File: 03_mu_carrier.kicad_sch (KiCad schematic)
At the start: 155 parts, among them J10 Amphenol MDT420M01001 M-key N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, J8 DNP Mu SIO UART debug header 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, Q750 BSS138 fail-off EN/UVLO clamp, Q751 BSS138 active-high enable rel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, SW2 Mu Power, SW3 Mu Reset, U6 TPS56637RPAR VSYS -> SYS_5V (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, U7 TPS56637RPAR VSYS -> SYS_3V3 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, U750 TPS552892RYQR 12V buck-boost, U769 SN74LVC1G08DBVR qualified hos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, U770 TPS2553DDBVR internal host VB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, U771 TPS3897ADRYR internal VBUS su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, U772 TPS22975NDSGR switched PCIe e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, U773 TPS56637RPAR VSYS -> PCIE_3V3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

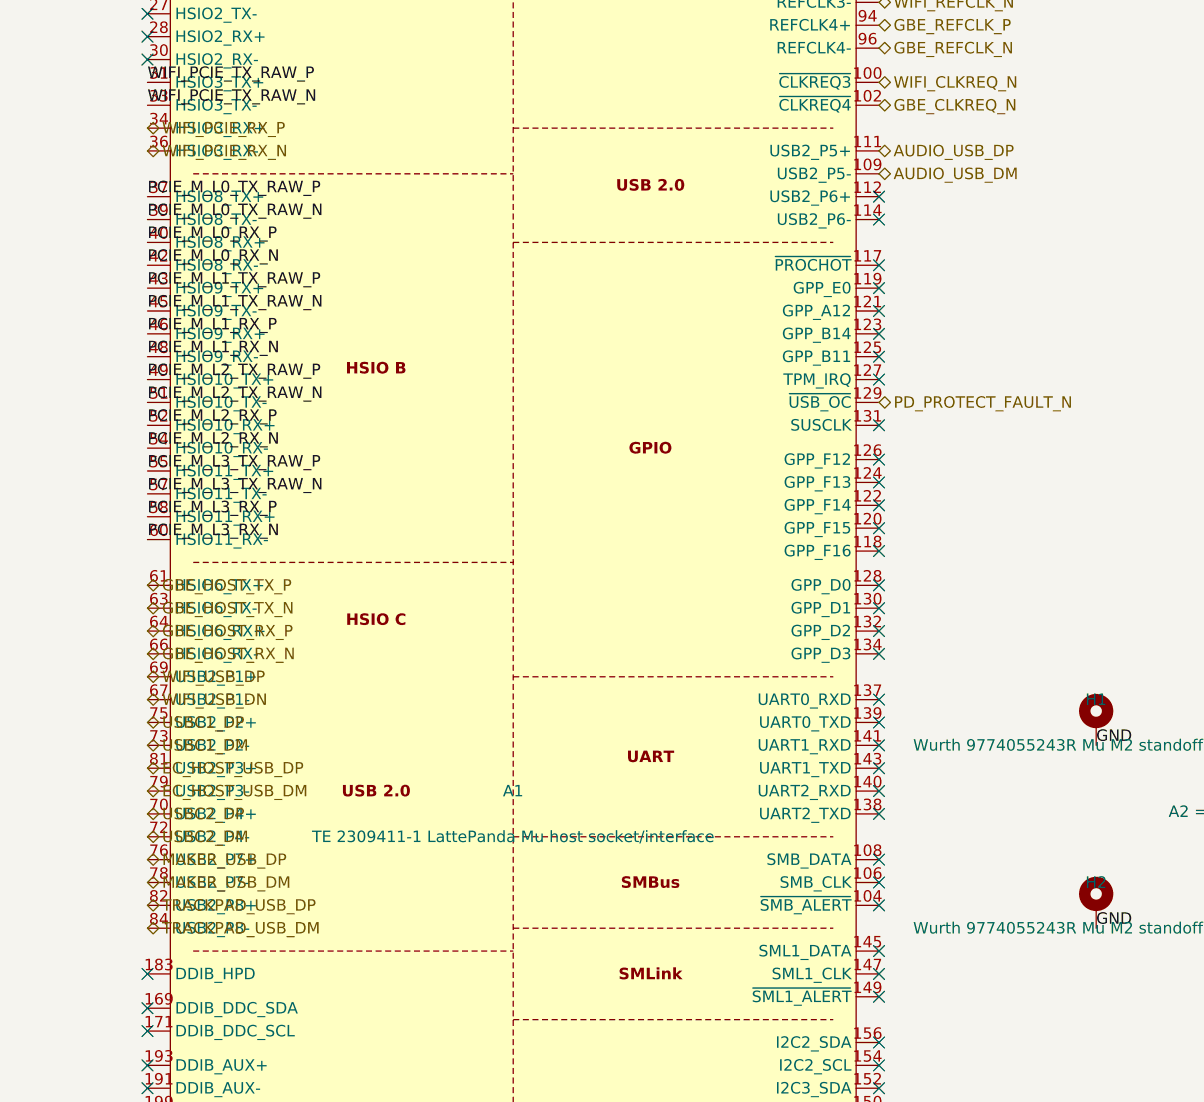
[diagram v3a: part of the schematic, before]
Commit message: get the main boards ready for routing
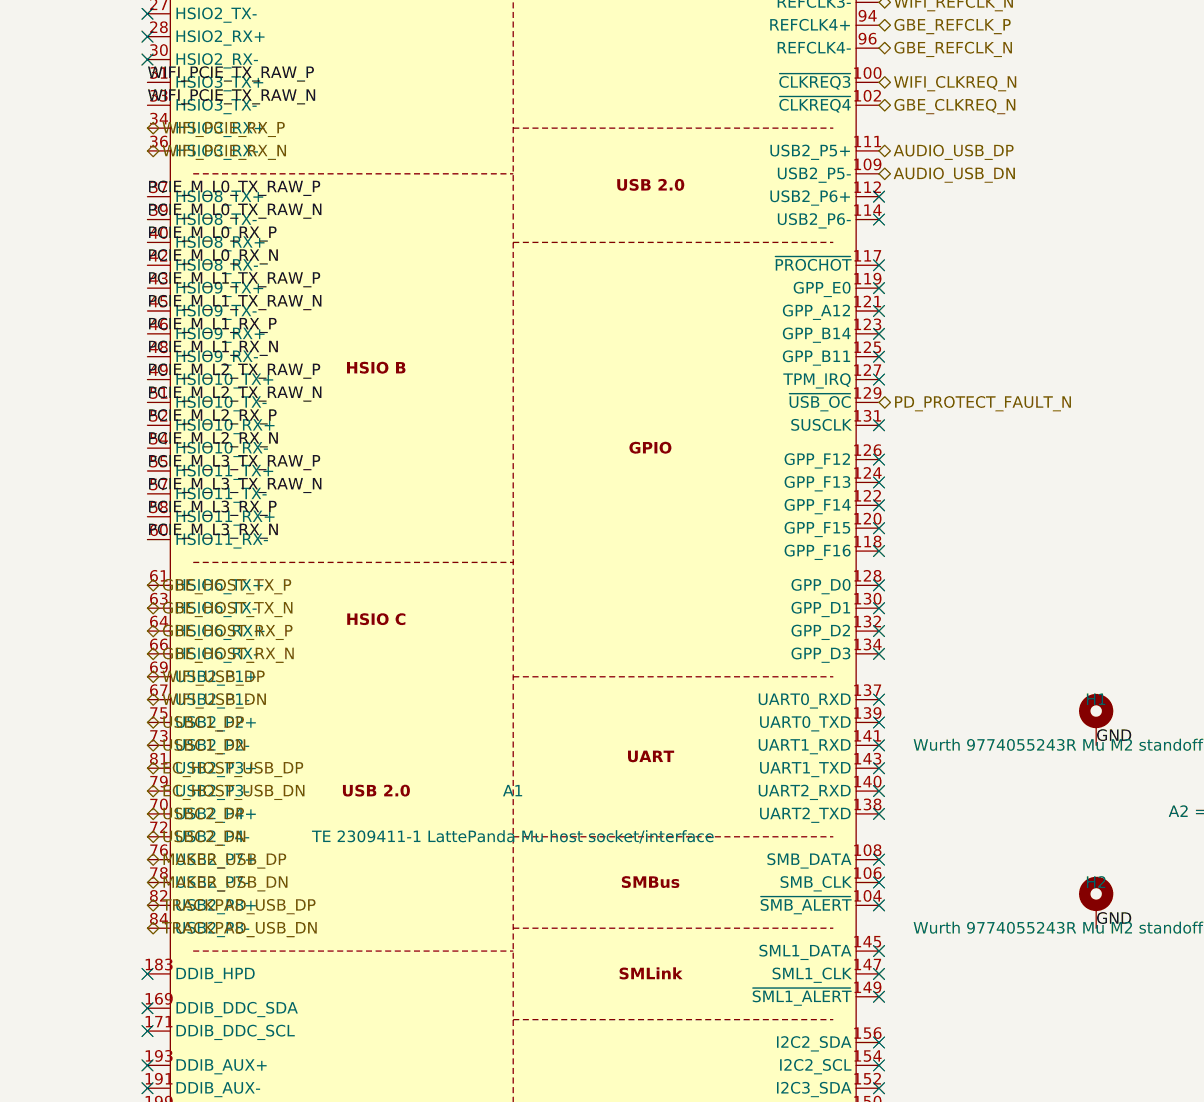
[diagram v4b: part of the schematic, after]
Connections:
- net AUDIO_USB_DM renamed AUDIO_USB_DN
- net EC_HOST_USB_DM renamed EC_HOST_USB_DN
- net MAKER_USB_DM renamed MAKER_USB_DN
- net TRACKPAD_USB_DM renamed TRACKPAD_USB_DN
- net USBC1_DM renamed USBC1_DN
- net USBC2_DM renamed USBC2_DN
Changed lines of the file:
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@@
 (no_connect (at 200.66 187.96))
 (no_connect (at 200.66 185.42))
-(hierarchical_label "AUDIO_USB_DM"
+(hierarchical_label "AUDIO_USB_DN"
   (shape bidirectional)
   (at 200.66 109.22 0)
@@
   (effects (font (size 1.27 1.27)) (justify left bottom))
 )
-(hierarchical_label "USBC2_DM"
+(hierarchical_label "USBC2_DN"
   (shape bidirectional)
   (at 119.38 182.88 0)
   (effects (font (size 1.27 1.27)) (justify left bottom))
 )
-(hierarchical_label "USBC1_DM"
+(hierarchical_label "USBC1_DN"
   (shape bidirectional)
   (at 119.38 172.72 0)
@@
   (effects (font (size 1.27 1.27)) (justify left bottom))
 )
-(hierarchical_label "MAKER_USB_DM"
+(hierarchical_label "MAKER_USB_DN"
   (shape bidirectional)
   (at 119.38 187.96 0)
   (effects (font (size 1.27 1.27)) (justify left bottom))
 )
-(hierarchical_label "EC_HOST_USB_DM"
+(hierarchical_label "EC_HOST_USB_DN"
   (shape bidirectional)
   (at 119.38 177.8 0)
@@
   (effects (font (size 1.27 1.27)) (justify left bottom))
 )
-(hierarchical_label "TRACKPAD_USB_DM"
+(hierarchical_label "TRACKPAD_USB_DN"
   (shape bidirectional)
   (at 119.38 193.04 0)

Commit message: fix audit issues and move some connectors
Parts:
- C762: footprint Capacitor_SMD:CP_Elec_6.3x5.8 -> Capacitor_SMD:CP_Elec_6.3x7.7
- C771: value 4.7n COMP -> 220n 50V X7R COMP; MPN GRM188R71H472KA01 -> C0603C224K5RACTU; Manufacturer Murata -> KEMET
- C772: value 100p C0G COMP HF -> 1n 50V C0G COMP HF; MPN GRM1885C1H101JA01 -> GRM1885C1H102JA01D
- C782, C834: footprint Capacitor_SMD:C_1206_3216Metric -> Capacitor_SMD:C_1210_3225Metric
- C783, C794, C832: footprint Capacitor_SMD:C_0805_2012Metric -> Capacitor_SMD:C_0603_1608Metric
- C830, C836: footprint Capacitor_SMD:C_1206_3216Metric -> Capacitor_SMD:C_0805_2012Metric
- D1824: value 1N5819HW RTC_BAT diode-OR from MCU_3V3 -> 1N5819HW RTC supply from MCU_3V3; footprint Diode_SMD:Nexperia_CFP3_SOD-123W -> Diode_SMD:D_SOD-123; MPN 1N5819HW -> 1N5819HW-7-F; Manufacturer STMicroelectronics -> Diodes Incorporated
- L750: value 4.7uH 10.1A Isat / 6.9A Irms -> 6.8uH 12.8A Isat30 / 6.8A Irms20; 7mm class; footprint Inductor_SMD:L_Coilcraft_XAL7030-472 -> Inductor_SMD:L_Coilcraft_XAL7070-XXX; MPN XAL7030-472MEC -> XAL7070-682MEC
- R40: MPN RT0603BRD075KL -> RT0603BRD0775KL
- R42, R770: MPN RC0603FR-07169KL -> RC0603FR-07100KL
- R45, R771: MPN RC0603FR-0736K1L -> RC0603FR-07100KL
- R755: value 15k COMP series -> 5.1k 1% COMP series; MPN RC0603FR-0715KL -> RC0603FR-075K1L
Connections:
- net MCU_3V3: now also D1824.2 (A); no longer D1824.1 (K)
- net RTC_BAT: now also D1824.1 (K); no longer D1824.2 (A)

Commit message: fix the center layout and more board issues
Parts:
- removed C40, C41: 10u 50V X7R TPS56637 VIN, Capacitor_SMD:C_1206_3216Metric, symbol Device:C
- removed C42: 100n 50V X7R TPS56637 VIN HF, Capacitor_SMD:C_0603_1608Metric, symbol Device:C
- removed C43: 100n 16V X7R TPS56637 BOOT, Capacitor_SMD:C_0603_1608Metric, symbol Device:C
- removed C44, C45: 22u 16V X7R TPS56637 OUT, Capacitor_SMD:C_1206_3216Metric, symbol Device:C
- removed C768: DNP 2.2n 250V X7R switch-node snubber, Capacitor_SMD:C_0805_2012Metric, symbol Device:C
- removed C794: 1u internal host VBUS switch input, Capacitor_SMD:C_0603_1608Metric, symbol Device:C
- removed C830: 10u internal host VBUS output, Capacitor_SMD:C_0805_2012Metric, symbol Device:C
- removed C834: 47u 6.3V PCIe endpoint rail bulk, Capacitor_SMD:C_1210_3225Metric, symbol Device:C
- removed C835: 100n PCIe endpoint rail HF, Capacitor_SMD:C_0603_1608Metric, symbol Device:C
- removed R761: 100k fail-off gate divider low, Resistor_SMD:R_0603_1608Metric, symbol Device:R
- removed R766: 100k fail-off gate divider high, Resistor_SMD:R_0603_1608Metric, symbol Device:R
- removed R787: 100k 1% TPS56637 EN high (host-active gate), Resistor_SMD:R_0603_1608Metric, symbol Device:R
- removed R788: 100k 1% TPS56637 EN low, Resistor_SMD:R_0603_1608Metric, symbol Device:R
- removed R789: 100k PCIE_3V3_PG pull-up, Resistor_SMD:R_0603_1608Metric, symbol Device:R
- removed U6: TPS56637RPAR VSYS -> SYS_5V (5.10V, 6A class), ducktop2:Texas_RPA0010A_VQFN-HR-10_3x3mm, symbol TPS56637:TPS56637
- removed U771: TPS3897ADRYR internal VBUS supervisor (always-pow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, Package_SON:Texas_USON-6_1x1.45mm_P0.5mm_SMD, symbol TPS3897ADRYR:TPS3897ADRYR
- removed U772: TPS22975NDSGR switched PCIe endpoint 3V3, Package_SON:Texas_DSG0008A_WSON-8-1EP_2x2mm_P0.5mm_EP0.9x1.6mm, symbol TPS22975N:TPS22975N
- removed U773: TPS56637RPAR VSYS -> PCIE_3V3_IN (3.32V, 6A class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, ducktop2:Texas_RPA0010A_VQFN-HR-10_3x3mm, symbol TPS56637:TPS56637
- added C2280: 22u 25V endpoint VCC; effective minimum 4.7u, Capacitor_SMD:C_1210_3225Metric, symbol Device:C
- added C2281: 100n 50V endpoint VDDA, Capacitor_SMD:C_0603_1608Metric, symbol Device:C
- added C2282: 220n 50V X7R endpoint COMP, Capacitor_SMD:C_0603_1608Metric, symbol Device:C
- added C2283: 2.2n 50V C0G endpoint COMP HF, Capacitor_SMD:C_0603_1608Metric, symbol Device:C
- added C2284, C2285: 330u 10V endpoint local reservoir, Capacitor_Tantalum_SMD:CP_EIA-7343-43_Kemet-X, symbol Device:C_Polarized
- added C2286, C778: 100n 50V endpoint input HF, Capacitor_SMD:C_0603_1608Metric, symbol Device:C
- added C2287: 22u 25V endpoint output; TI characterized part, Capacitor_SMD:C_1210_3225Metric, symbol Device:C
- added C2288: 100n 50V endpoint enable gate supply, Capacitor_SMD:C_0603_1608Metric, symbol Device:C
- added C2289: 22n 50V C0G 5% endpoint slew; parallel pair, Capacitor_SMD:C_0805_2012Metric, symbol Device:C
- added C2412: 100n, Capacitor_SMD:C_0603_1608Metric, symbol Device:C
- added C46, C790: 10u 50V X7R TPS56637 VIN, Capacitor_SMD:C_1206_3216Metric, symbol Device:C
- added C47: 100n 16V X7R TPS56637 BOOT, Capacitor_SMD:C_0603_1608Metric, symbol Device:C
- added C48, C792: 22u 25V X7R TPS56637 OUT; TI example part, Capacitor_SMD:C_1210_3225Metric, symbol Device:C
- added C586, C587, C66, C67: 100n 10V X7R Mu USB3 TX AC, Capacitor_SMD:C_0402_1005Metric, symbol Device:C
- added C776, C777: 10u 50V endpoint input, Capacitor_SMD:C_1206_3216Metric, symbol Device:C
- added C791: 100n 50V X7R TPS56637 VIN HF, Capacitor_SMD:C_0603_1608Metric, symbol Device:C
- added H25: M2.5 isolated mainboard mounting hole, MountingHole:MountingHole_2.7mm_M2.5, symbol Mechanical:MountingHole
- added J10: Amphenol MDT420M01001 M-key NVMe socket (PCIe x4), ducktop2:Amphenol_MDT420M01001_H4.2, symbol Connector:Bus_M.2_Socket_M
- added L5: XAL7070-222MEC 2.2uH 19.6A Isat30%, Inductor_SMD:L_Coilcraft_XAL7070-XXX, symbol Device:L
- added Q751: BSS138 active-high enable release, Package_TO_SOT_SMD:SOT-23, symbol Q_NMOS_SOT23_GSD:Q_NMOS_SOT23_GSD
- added R2282: 3.3k endpoint COMP, Resistor_SMD:R_0603_1608Metric, symbol Device:R
- added R2283: 1R endpoint BOOT damping, Resistor_SMD:R_0603_1608Metric, symbol Device:R
- added R2290: 100R 1% 0.25W endpoint QOD discharge, Resistor_SMD:R_1206_3216Metric, symbol Device:R
- added R2291: 100k endpoint load-switch PG pull-up, Resistor_SMD:R_0603_1608Metric, symbol Device:R
- added R2292: 10mOhm 1% 1W NVMe branch damping, ducktop2:Panasonic_ERJ8CW_10to16m_Center, symbol Device:R
- added R2428: 10k, Resistor_SMD:R_0603_1608Metric, symbol Device:R
- added R43: 45.3k 0.02% 5ppm TPS56637 FB high, Resistor_SMD:R_0603_1608Metric, symbol Device:R
- added R44: 10k 0.02% 5ppm TPS56637 FB low, Resistor_SMD:R_0603_1608Metric, symbol Device:R
- added R47: 0R / PERST isolation, Resistor_SMD:R_0603_1608Metric, symbol Device:R
- added R48: 0R / REFCLK+ isolation, Resistor_SMD:R_0603_1608Metric, symbol Device:R
- added R49: 0R / REFCLK- isolation, Resistor_SMD:R_0603_1608Metric, symbol Device:R
- added R50: 1k NVMe CLKREQ# low: request REFCLK, Resistor_SMD:R_0603_1608Metric, symbol Device:R
- added R762: 100k PG pull-up, Resistor_SMD:R_0603_1608Metric, symbol Device:R
- added R770: 100k 1% TPS56637 EN high (host-active gate), Resistor_SMD:R_0603_1608Metric, symbol Device:R
- added R771: 100k 1% TPS56637 EN low, Resistor_SMD:R_0603_1608Metric, symbol Device:R
- added R772: 100k SYS_3V3 PG pull-up, Resistor_SMD:R_0603_1608Metric, symbol Device:R
- added R778: 10.0k 1% VBUS sense bottom divider, Resistor_SMD:R_0603_1608Metric, symbol Device:R
- added RS2280, RS2281: 13mOhm 1% 1W; parallel pair gives 6.5mOhm, ducktop2:Panasonic_ERJ8CW_10to16m_Center, symbol Device:R
- added RS2360, RS2361: 10mOhm 1% 1W; parallel pair gives 5mOhm, ducktop2:Panasonic_ERJ8CW_10to16m_Center, symbol Device:R
- added TP13: Internal USB VBUS test, TestPoint:TestPoint_Pad_D1.0mm, symbol Connector:TestPoint
- added TP2280: PCIE_LOAD_PG, TestPoint:TestPoint_Pad_1.5x1.5mm, symbol Connector:TestPoint
- added U2280: SN74LVC1G08DBVR endpoint PG-qualified enable, Package_TO_SOT_SMD:SOT-23-5, symbol 74xGxx:74LVC1G08
- added U2412: SN74LVC1G08DBVR SYS5 PG and actual VBUS qualify, Package_TO_SOT_SMD:SOT-23-5, symbol 74xGxx:74LVC1G08
- added U6: LM706A0RRXR SYS_5V 5.106V; 4.5A envelope, ducktop2:Texas_RRX0029B_VQFN-29_6x6mm, symbol LM706A0:LM706A0
- added U772: TPS22992SRXNR endpoint slew and short protection, ducktop2:Texas_RXN0008A_WQFN-HR-8_1.25x1.25mm, symbol TPS22992S:TPS22992S
- C2360: renamed from C792; value 22u 16V X7R TPS56637 OUT -> 22u 25V SYS5 VCC; effective minimum 4.7u; footprint Capacitor_SMD:C_1206_3216Metric -> Capacitor_SMD:C_1210_3225Metric; MPN GRM31CZ71C226ME15L -> GRM32ER71E226KE15L
- C2361: renamed from C66; value 100n 10V X7R Mu USB3 TX AC -> 100n 50V SYS5 VDDA; footprint Capacitor_SMD:C_0402_1005Metric -> Capacitor_SMD:C_0603_1608Metric; MPN GRM155R71A104KA01D -> GRM188R71H104KA93D
- C2362: renamed from C47; value 100n 16V X7R TPS56637 BOOT -> 220n 50V X7R SYS5 COMP; MPN C1608X7R1C104K080AA -> C0603C224K5RACTU; Manufacturer TDK -> KEMET
- C2363: renamed from L5; value XAL7070-222MEC 2.2uH 19.6A Isat30% -> 2.2n 50V C0G SYS5 COMP HF; footprint Inductor_SMD:L_Coilcraft_XAL7070-XXX -> Capacitor_SMD:C_0603_1608Metric; symbol Device:L -> Device:C; MPN XAL7070-222MEC -> C0603C222J5GACTU; Manufacturer Coilcraft -> KEMET
- C2364: renamed from C587; value 100n 10V X7R Mu USB3 TX AC -> 220u 10V SYS5 local reservoir; 6mOhm; footprint Capacitor_SMD:C_0402_1005Metric -> Capacitor_Tantalum_SMD:CP_EIA-7343-31_Kemet-D; symbol Device:C -> Device:C_Polarized; HeightMax (none) -> 3.1mm; MPN GRM155R71A104KA01D -> T530D227M010ATE006; Manufacturer Murata -> KEMET
- C2365: renamed from C48; value 22u 16V X7R TPS56637 OUT -> 100n 50V SYS5 input HF; footprint Capacitor_SMD:C_1206_3216Metric -> Capacitor_SMD:C_0603_1608Metric; MPN GRM31CZ71C226ME15L -> GRM188R71H104KA93D
- C40: renamed from R770; value 100k 1% TPS56637 EN high (host-active gate) -> 10u 50V SYS5 input; footprint Resistor_SMD:R_0603_1608Metric -> Capacitor_SMD:C_1206_3216Metric; symbol Device:R -> Device:C; MPN RC0603FR-07100KL -> CGA5L1X7R1H106K160AC; Manufacturer Yageo -> TDK
- C41: renamed from R771; value 100k 1% TPS56637 EN low -> 10u 50V SYS5 input; footprint Resistor_SMD:R_0603_1608Metric -> Capacitor_SMD:C_1206_3216Metric; symbol Device:R -> Device:C; MPN RC0603FR-07100KL -> CGA5L1X7R1H106K160AC; Manufacturer Yageo -> TDK
- C42: renamed from R772; value 100k SYS_3V3 PG pull-up -> 100n 50V SYS5 input HF; footprint Resistor_SMD:R_0603_1608Metric -> Capacitor_SMD:C_0603_1608Metric; symbol Device:R -> Device:C; MPN RC0603FR-07100KL -> GRM188R71H104KA93D; Manufacturer Yageo -> Murata
- C43: renamed from R44; value 10k 1% TPS56637 FB low -> 47n 25V SYS5 bootstrap; footprint Resistor_SMD:R_0603_1608Metric -> Capacitor_SMD:C_0402_1005Metric; symbol Device:R -> Device:C; MPN RC0603FR-0710KL -> GRM155R71E473KA88D; Manufacturer Yageo -> Murata
- C44: renamed from C67; value 100n 10V X7R Mu USB3 TX AC -> 22u 25V SYS5 output; TI characterized part; footprint Capacitor_SMD:C_0402_1005Metric -> Capacitor_SMD:C_1210_3225Metric; MPN GRM155R71A104KA01D -> GRM32ER71E226KE15L
- C45: renamed from C586; value 100n 10V X7R Mu USB3 TX AC -> 22u 25V SYS5 output; TI characterized part; footprint Capacitor_SMD:C_0402_1005Metric -> Capacitor_SMD:C_1210_3225Metric; MPN GRM155R71A104KA01D -> GRM32ER71E226KE15L
- C768: renamed from Q751; value BSS138 active-high enable release -> DNP 2.2n 250V X7R switch-node snubber; footprint Package_TO_SOT_SMD:SOT-23 -> Capacitor_SMD:C_0805_2012Metric; symbol Q_NMOS_SOT23_GSD:Q_NMOS_SOT23_GSD -> Device:C; MPN BSS138LT1G -> GRM21AR72E222KW01D; Manufacturer onsemi -> Murata; now not fitted; now left out of the parts list
- C771: value 220n 50V X7R COMP -> 330n 50V X7R COMP; effective 210..500nF; MPN C0603C224K5RACTU -> CGA3E3X7R1H334K080AB; Manufacturer KEMET -> TDK
- C779: value 100n 16V X7R TPS56637 BOOT -> 47n 25V endpoint bootstrap; footprint Capacitor_SMD:C_0603_1608Metric -> Capacitor_SMD:C_0402_1005Metric; MPN C1608X7R1C104K080AA -> GRM155R71E473KA88D; Manufacturer TDK -> Murata
- C782: value 47u 6.3V PCIE_3V3_IN rail bulk -> 22u 25V endpoint output; TI characterized part; MPN GRM32ER60J476ME20L -> GRM32ER71E226KE15L
- C794: renamed from C776; value 10u 50V X7R TPS56637 VIN -> 1u internal host VBUS switch input; footprint Capacitor_SMD:C_1206_3216Metric -> Capacitor_SMD:C_0603_1608Metric; MPN CGA5L1X7R1H106K160AC -> GRM188R71A105KA61D; Manufacturer TDK -> Murata
- C830: renamed from C777; value 10u 50V X7R TPS56637 VIN -> 10u internal host VBUS output; footprint Capacitor_SMD:C_1206_3216Metric -> Capacitor_SMD:C_0805_2012Metric; MPN CGA5L1X7R1H106K160AC -> GRM21BR61A106KE19L; Manufacturer TDK -> Murata
- C832: value 1u PCIe endpoint switch input -> 1u endpoint switch input
- C833: value 4.7n PCIe endpoint controlled slew -> 22n 50V C0G 5% endpoint slew; parallel pair; footprint Capacitor_SMD:C_0402_1005Metric -> Capacitor_SMD:C_0805_2012Metric; MPN GRM155R71H472KA01D -> C0805C223J5GACTU; Manufacturer Murata -> KEMET
- C834: renamed from H14; value M2.5 isolated mainboard mounting hole -> 22u 25V NVMe local bulk; TI characterized part; footprint MountingHole:MountingHole_2.7mm_M2.5 -> Capacitor_SMD:C_1210_3225Metric; symbol Mechanical:MountingHole -> Device:C; Hardware_Spec 2.7mm isolated NPTH for M2.5 chassis screw; no electrical c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 -> (none); MPN (none) -> GRM32ER71E226KE15L; Manufacturer (none) -> Murata; now in the parts list
- C835: renamed from H25; value M2.5 isolated mainboard mounting hole -> 100n NVMe rail HF; footprint MountingHole:MountingHole_2.7mm_M2.5 -> Capacitor_SMD:C_0603_1608Metric; symbol Mechanical:MountingHole -> Device:C; Hardware_Spec 2.7mm isolated NPTH for M2.5 chassis screw; no electrical c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 -> (none); MPN (none) -> GRM188R71A104KA01D; Manufacturer (none) -> Murata; now in the parts list
- L1702: value XAL7070-222MEC 2.2uH 19.6A Isat30% -> 8.2uH 16.9A Isat30; endpoint; footprint Inductor_SMD:L_Coilcraft_XAL7070-XXX -> ducktop2:Coilcraft_XGL1060_Center; Layout (none) -> pad1_marked_short_lead_to_SW;6mm_max_height; MPN XAL7070-222MEC -> XGL1060-822MEC
- L4: value XAL7070-332MEC 3.3uH 19.4A Isat30% -> 6.8uH 18.4A Isat30; SYS_5V; footprint Inductor_SMD:L_Coilcraft_XAL7070-XXX -> ducktop2:Coilcraft_XGL1060_Center; Layout (none) -> pad1_marked_short_lead_to_SW;6mm_max_height; MPN XAL7070-332MEC -> XGL1060-682MEC
- L750: value 6.8uH 12.8A Isat30 / 6.8A Irms20; 7mm class -> 6.8uH 18.4A Isat30 / 10.9A Irms20; 6mm max; footprint Inductor_SMD:L_Coilcraft_XAL7070-XXX -> ducktop2:Coilcraft_XGL1060_Center; MPN XAL7070-682MEC -> XGL1060-682MEC
- R2280: renamed from R50; value 1k NVMe CLKREQ# low: request REFCLK -> 22.1k 0.02% 5ppm endpoint RT; ClockPolicy Requests REFCLK; Mu BIOS/device-presence policy still contr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 -> (none); MPN RC0603FR-071KL -> TNPU060322K1HZEN00; Manufacturer Yageo -> Vishay
- R2281: renamed from J10; value Amphenol MDT420M01001 M-key NVMe socket (PCIe x4) -> 29.4k endpoint standalone config; footprint ducktop2:Amphenol_MDT420M01001_H4.2 -> Resistor_SMD:R_0603_1608Metric; symbol Connector:Bus_M.2_Socket_M -> Device:R; MPN MDT420M01001 -> RC0603FR-0729K4L; Manufacturer Amphenol -> Yageo
- R2360: renamed from C46; value 10u 50V X7R TPS56637 VIN -> 22.1k 0.02% 5ppm SYS5 RT; footprint Capacitor_SMD:C_1206_3216Metric -> Resistor_SMD:R_0603_1608Metric; symbol Device:C -> Device:R; MPN CGA5L1X7R1H106K160AC -> TNPU060322K1HZEN00; Manufacturer TDK -> Vishay
- R2361: renamed from C790; value 10u 50V X7R TPS56637 VIN -> 29.4k SYS5 standalone config; footprint Capacitor_SMD:C_1206_3216Metric -> Resistor_SMD:R_0603_1608Metric; symbol Device:C -> Device:R; MPN CGA5L1X7R1H106K160AC -> RC0603FR-0729K4L; Manufacturer TDK -> Yageo
- R2362: renamed from C791; value 100n 50V X7R TPS56637 VIN HF -> 2.2k SYS5 COMP; footprint Capacitor_SMD:C_0603_1608Metric -> Resistor_SMD:R_0603_1608Metric; symbol Device:C -> Device:R; MPN GRM188R71H104KA93D -> TNPU06032K20HZEN00; Manufacturer Murata -> Vishay
- R2363: renamed from R43; value 45.3k 1% TPS56637 FB high -> 1R SYS5 BOOT damping; MPN RC0603FR-0745K3L -> RC0603FR-071RL
- R40: value 75.0k 0.1% TPS56637 FB high -> 54.9k 0.02% 5ppm SYS5 FB high; MPN RT0603BRD0775KL -> TNPU060354K9HZEN00; Manufacturer Yageo -> Vishay
- R41: value 10k 0.1% TPS56637 FB low -> 10.2k 0.02% 5ppm SYS5 FB low; MPN RT0603BRD0710KL -> TNPU060310K2HZEN00; Manufacturer Yageo -> Vishay
- R42: value 100k 1% TPS56637 EN high (host-active gate) -> 100k 1% SYS5 EN high
- R45: value 100k 1% TPS56637 EN low -> 100k 1% SYS5 EN low
- R753: value 102k 0.1% 12V FB high -> 102k 0.1% 10ppm 12V FB high; MPN RT0603BRD07102KL -> TNPW0603102KBYEA; Manufacturer Yageo -> Vishay
- R754: value 11.3k 0.1% 12V FB low -> 11.3k 0.02% 5ppm 12V FB low; MPN RT0603BRD0711K3L -> TNPU060311K3HZEN00; Manufacturer Yageo -> Vishay
- R755: value 5.1k 1% COMP series -> 5.1k 0.02% 5ppm COMP series; MPN RC0603FR-075K1L -> TNPU06035K10HZEN00; Manufacturer Yageo -> Vishay
- R756: value 49.9k 1% FSW = 400kHz -> 49.9k 0.02% 5ppm FSW = 400kHz; MPN RC0603FR-0749K9L -> TNPU060349K9HZEN00; Manufacturer Yageo -> Vishay
- R759: value 150k 1% UVLO high; 9.0V rising -> 150k 0.1% 10ppm UVLO high; 9.0V rising; MPN RC0603FR-07150KL -> TNPW0603150KBYEA; Manufacturer Yageo -> Vishay
- R760: value 23.7k 1% UVLO low -> 23.7k 0.02% 5ppm UVLO low; MPN RC0603FR-0723K7L -> TNPU060323K7HZEN00; Manufacturer Yageo -> Vishay
- R761: renamed from R778; value 10.0k 1% VBUS sense bottom divider -> 100k fail-off gate divider low; MPN RC0603FR-0710KL -> RC0603FR-07100KL
- R766: renamed from TP13; value Internal USB VBUS test -> 100k fail-off gate divider high; footprint TestPoint:TestPoint_Pad_D1.0mm -> Resistor_SMD:R_0603_1608Metric; symbol Connector:TestPoint -> Device:R; MPN (none) -> RC0603FR-07100KL; Manufacturer (none) -> Yageo; ProcurementClass PCB copper test feature -> (none); now in the parts list
- R776: value 100k PCIe endpoint rail fail-low -> 10k endpoint switch fail-low; MPN RC0603FR-07100KL -> RC0603FR-0710KL
- R785: value 45.3k 1% TPS56637 FB high -> 32.4k 0.02% 5ppm endpoint FB high; MPN RT0603BRD0745K3L -> TNPU060332K4HZEN00; Manufacturer Yageo -> Vishay
- R786: value 10k 1% TPS56637 FB low -> 10k 0.02% 5ppm endpoint FB low; MPN RT0603BRD0710KL -> TNPU060310K0HZEN00; Manufacturer Yageo -> Vishay
- R787: renamed from R47; value 0R / PERST isolation -> 100k endpoint EN top; MPN RC0603FR-070RL -> RC0603FR-07100KL
- R788: renamed from R48; value 0R / REFCLK+ isolation -> 100k endpoint EN bottom; MPN RC0603FR-070RL -> RC0603FR-07100KL
- R789: renamed from R49; value 0R / REFCLK- isolation -> 10k endpoint converter PG pull-up; MPN RC0603FR-070RL -> RC0603FR-0710KL
- RS750: value 15mOhm 1% 1W; 3.33A output current limit -> 13mOhm 1% 1W; 3.85A nominal limit, 3.3A operating envelope; footprint Resistor_SMD:R_1206_3216Metric -> ducktop2:Panasonic_ERJ8CW_10to16m_Center; MPN ERJ8BWFR015V -> ERJ8CWFR013V
- U771: renamed from C778; value 100n 50V X7R TPS56637 VIN HF -> TPS3897ADRYR internal VBUS supervisor (always-powered); footprint Capacitor_SMD:C_0603_1608Metric -> Package_SON:Texas_USON-6_1x1.45mm_P0.5mm_SMD; symbol Device:C -> TPS3897ADRYR:TPS3897ADRYR; Function (none) -> Assert VBUS valid only after SENSE (divided INTERNAL_USB_VB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; MPN GRM188R71H104KA93D -> TPS3897ADRYR; Manufacturer Murata -> Texas Instruments
- U773: renamed from R762; value 100k PG pull-up -> LM706A0RRXR endpoint 3.392V; 5A continuous envelope; footprint Resistor_SMD:R_0603_1608Metric -> ducktop2:Texas_RRX0029B_VQFN-29_6x6mm; symbol Device:R -> LM706A0:LM706A0; Compensation (none) -> 3.3k+220n;2.2nHF;0.95MHz;local300..1500uF;endpoint10..2000uF; Layout (none) -> local_power_return;module_branch_L_le150nH;Kelvin_shunt_pai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; MPN RC0603FR-07100KL -> LM706A0RRXR; Manufacturer Yageo -> Texas Instruments
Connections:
- net BUCK33_BOOT: now also C47.1; no longer C2362.1
- net BUCK33_EN: now also R770.2, R771.1; no longer C40.2, C41.1
- net BUCK33_FB: now also R43.2, R44.1; no longer C43.1, R2363.2
- net BUCK33_SW: now also C47.2, L5.1; no longer C2362.2, C2363.1
- net BUCK5_BOOT: now also R2363.1, U6.4 (CBOOT)
- net BUCK5_EN: now also U6.9 (EN/UVLO)
- net BUCK5_FB: now also U6.16 (FB)
- net BUCK5_SW: now also U6.20 (SW1), U6.21 (SW2), U6.22 (SW3)
- net BUCKPE_BOOT: now also U773.4 (CBOOT), R2283.1; no longer C779.1
- net BUCKPE_EN: now also R787.2, R788.1, U773.9 (EN/UVLO)
- net BUCKPE_FB: now also U773.16 (FB)
- net BUCKPE_SW: now also U773.20 (SW1), U773.21 (SW2), U773.22 (SW3); no longer C779.2
- net GND: now also C2361.2, C2362.2, C2363.2, C2364.2, C40.2, C42.2, C44.2, C45.2, C834.2, C835.2, R2281.2, R788.2, U773.17 (AGND), U773.23 (PGND1), U773.24 (PGND2), U773.25 (PGND3), U773.26 (PGND4), U773.30 (PGND), U773.6 (BIAS), U773.8 (PFM/SYNCIN), C2280.2, C2281.2, C2282.2, C2283.2, C2284.2, C2285.2, C2286.2, C2287.2, C2288.2, C2289.2, C2412.2, C46.2, C48.2, C776.2, C777.2, C778.2, C790.2, C791.2, C792.2, J10.1 (GND), J10.15 (GND), J10.21 (GND), J10.27 (GND), J10.3 (GND), J10.33 (GND), J10.39 (GND), J10.45 (GND), J10.51 (GND), J10.57 (GND), J10.71 (GND), J10.73 (GND), J10.75 (GND), J10.9 (GND), Q751.2 (S), R2428.2, R44.2, R50.2, R771.2, R778.2, U2280.3 (GND), U2412.3 (GND), U6.17 (AGND), U6.23 (PGND1), U6.24 (PGND2), U6.25 (PGND3), U6.26 (PGND4), U6.30 (PGND), U6.6 (BIAS), U6.8 (PFM/SYNCIN), U772.4 (GND); no longer C43.2, R2281.1 (GND), R2281.15 (GND), R2281.21 (GND), R2281.27 (GND), R2281.3 (GND), R2281.33 (GND), R2281.39 (GND), R2281.45 (GND), R2281.51 (GND), R2281.57 (GND), R2281.71 (GND), R2281.73 (GND), R2281.75 (GND), R2281.9 (GND), R2362.2
- net INTERNAL_USB_VBUS: now also C830.1, TP13.1; no longer R766.1
- net INTERNAL_USB_VBUS_SENSE: now also U771.3 (SENSE), R778.1; no longer R761.1
- net INTERNAL_USB_VBUS_VALID: now also R2428.1, U2412.4; no longer R775.2
- net MCU_3V3: now also R789.1, U771.1 (ENABLE), U771.6 (VCC), C2288.1, C2412.1, R762.1, R772.1, U2280.5 (VCC), U2412.5 (VCC); no longer C42.1, U773.1
- net MU12_FORCE_OFF: now also R761.1, R766.2, Q751.3 (D); no longer C768.3 (D)
- net MU12_SNUB1: now also C768.1
- net MU_12V_ENABLE: now also Q751.1 (G); no longer C768.1 (G)
- net MU_12V_PG: now also R762.2; no longer U773.2
- net MU_HOST_ACTIVE: now also R787.1, R770.1, U2280.1; no longer C40.1, R776.1
- net PCIE_3V3: now also R2290.1, R2291.1, R2292.1, U772.6 (VOUT); no longer C836.1, C837.1, R2281.12 (3.3V), R2281.14 (3.3V), R2281.16 (3.3V), R2281.18 (3.3V), R2281.2 (3.3V), R2281.4 (3.3V), R2281.70 (3.3V), R2281.72 (3.3V), R2281.74 (3.3V)
- net PCIE_3V3_CT: now also C2289.1, U772.7 (CT)
- net PCIE_3V3_IN: now also U773.12 (VOUT), C2284.1, C2285.1, C2287.1, RS2280.2, RS2281.2, U772.1 (VBIAS), U772.2 (VIN); no longer L1702.2
- net PCIE_3V3_PG: now also R789.2, U773.7 (PG/SYNCOUT), U2280.2
- net PCIE_M_CLKREQ_N: now also J10.52 (~{CLKREQ}), R50.1; no longer R2280.1, R2281.52 (~{CLKREQ})
- net PCIE_M_L0_RX_N: now also J10.41 (PERn0/SATA-B+); no longer R2281.41 (PERn0/SATA-B+)
- net PCIE_M_L0_RX_P: now also J10.43 (PERp0/SATA-B-); no longer R2281.43 (PERp0/SATA-B-)
- net PCIE_M_L0_TX_N: now also J10.47 (PETn0/SATA-A-); no longer R2281.47 (PETn0/SATA-A-)
- net PCIE_M_L0_TX_P: now also J10.49 (PETp0/SATA-A+); no longer R2281.49 (PETp0/SATA-A+)
- net PCIE_M_L1_RX_N: now also J10.29 (PERn1); no longer R2281.29 (PERn1)
- net PCIE_M_L1_RX_P: now also J10.31 (PERp1); no longer R2281.31 (PERp1)
- net PCIE_M_L1_TX_N: now also J10.35 (PETn1); no longer R2281.35 (PETn1)
- net PCIE_M_L1_TX_P: now also J10.37 (PETp1); no longer R2281.37 (PETp1)
- net PCIE_M_L2_RX_N: now also J10.17 (PERn2); no longer R2281.17 (PERn2)
- net PCIE_M_L2_RX_P: now also J10.19 (PERp2); no longer R2281.19 (PERp2)
- net PCIE_M_L2_TX_N: now also J10.23 (PETn2); no longer R2281.23 (PETn2)
- net PCIE_M_L2_TX_P: now also J10.25 (PETp2); no longer R2281.25 (PETp2)
- net PCIE_M_L3_RX_N: now also J10.5 (PERn3); no longer R2281.5 (PERn3)
- net PCIE_M_L3_RX_P: now also J10.7 (PERp3); no longer R2281.7 (PERp3)
- net PCIE_M_L3_TX_N: now also J10.11 (PETn3); no longer R2281.11 (PETn3)
- net PCIE_M_L3_TX_P: now also J10.13 (PETp3); no longer R2281.13 (PETp3)
- net PCIE_M_PERST_N: now also J10.50 (~{PERST}), R47.2; no longer R2281.50 (~{PERST}), R787.2
- net PCIE_M_REFCLK_N: now also J10.53 (REFCLKn), R49.2; no longer R2281.53 (REFCLKn), R789.2
- net PCIE_M_REFCLK_P: now also J10.55 (REFCLKp), R48.2; no longer R2281.55 (REFCLKp), R788.2
- net PCIE_M_REFCLK_SRC_N: now also R49.1; no longer R789.1
- net PCIE_M_REFCLK_SRC_P: now also R48.1; no longer R788.1
- net PCIE_WAKE_N: now also J10.54 (~{PEWAKE}); no longer R2281.54 (~{PEWAKE})
- net PLTRST_SRC_N: now also R47.1; no longer R787.1
- net SYS_3V3: now also C48.1, C792.1, L5.2, R43.1; no longer C2360.1, C2363.2, C2365.1, R2363.1
- net SYS_3V3_PG: now also R772.2; no longer C42.2
- net SYS_5V: now also C2364.1, C44.1, C45.1, C794.1, RS2360.2, RS2361.2, U6.12 (VOUT); no longer L4.2
- net SYS_5V_PG: now also U2412.1, U6.7 (PG/SYNCOUT)
- net USBC1_SSTX_N: now also C67.2; no longer C44.2
- net USBC1_SSTX_P: now also C66.2; no longer C2361.2
- net USBC1_SSTX_RAW_N: now also C67.1; no longer C44.1
- net USBC1_SSTX_RAW_P: now also C66.1; no longer C2361.1
- net USBC2_SSTX_N: now also C587.2; no longer C2364.2
- net USBC2_SSTX_P: now also C586.2; no longer C45.2
- net USBC2_SSTX_RAW_N: now also C587.1; no longer C2364.1
- net USBC2_SSTX_RAW_P: now also C586.1; no longer C45.1
- net VSYS: now also C2365.1, C40.1, C41.1, C42.1, R766.1, U773.1 (VIN4), U773.2 (VIN5), U773.27 (VIN1), U773.28 (VIN2), U773.29 (VIN3), U773.3 (VIN6), C2286.1, C46.1, C776.1, C777.1, C778.1, C790.1, C791.1, U6.1 (VIN4), U6.2 (VIN5), U6.27 (VIN1), U6.28 (VIN2), U6.29 (VIN3), U6.3 (VIN6); no longer C794.1, C830.1, R2360.1, R2361.1, R2362.1, U771.1
- new net BUCK5_BOOT_C: C43.1, R2363.2
- new net BUCK5_COMP: C2363.1, R2362.1, U6.15 (EXTCOMP)
- new net BUCK5_COMP_RC: C2362.1, R2362.2
- new net BUCK5_CONFIG: R2361.1, U6.13 (CONFIG)
- new net BUCK5_RT: R2360.1, U6.14 (RT)
- new net BUCK5_SW_BOOT: C43.2, U6.5 (SW4)
- new net BUCK5_VCC: C2360.1, U6.19 (VCC)
- new net BUCK5_VDDA: C2361.1, U6.18 (VDDA)
- new net BUCKPE_BOOT_C: C779.1, R2283.2
- new net BUCKPE_COMP: C2283.1, R2282.1, U773.15 (EXTCOMP)
- new net BUCKPE_COMP_RC: C2282.1, R2282.2
- new net BUCKPE_CONFIG: R2281.1, U773.13 (CONFIG)
- new net BUCKPE_RT: R2280.1, U773.14 (RT)
- new net BUCKPE_SW_BOOT: C779.2, U773.5 (SW4)
- new net BUCKPE_VCC: C2280.1, U773.19 (VCC)
- new net BUCKPE_VDDA: C2281.1, U773.18 (VDDA)
- new net INTERNAL_USB_VBUS_RAW_VALID: R775.2, U2412.2, U771.4 (SENSE_OUT)
- new net NVME_3V3: C834.1, C835.1, C836.1, C837.1, J10.12 (3.3V), J10.14 (3.3V), J10.16 (3.3V), J10.18 (3.3V), J10.2 (3.3V), J10.4 (3.3V), J10.70 (3.3V), J10.72 (3.3V), J10.74 (3.3V), R2292.2
- new net PCIE_LOAD_EN: R776.1, U2280.4, U772.8 (ON)
- new net PCIE_LOAD_PG: R2291.2, TP2280.1, U772.3 (PG)
- new net PCIE_PRE_SENSE: L1702.2, RS2280.1, RS2281.1, U773.11 (ISNS+)
- new net PCIE_QOD: R2290.2, U772.5 (QOD)
- new net SYS5_PRE_SENSE: L4.2, RS2360.1, RS2361.1, U6.11 (ISNS+)
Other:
- note added: "== SYS_5V: 4.5A continuous, complete switched-bank model =="
- note added: "SYS5: local ceramic <=80uF, polymer <=500uF, all switched branches <=300uF; 4.5A load plus startup. source admission remains separate."
- note added: "SYS_5V uses externally compensated LM706A0 at 4.5A; SYS_3V3 uses TPS56637 with a complete bank below 100uF. source admission remains separate."
- note added: "endpoint: local module-loop L <=150nH; total post-switch C <=2mF including board parts; 5A DC plus <=0.4A inrush; qualify transients."
- note removed: "SYS_5V and SYS_3V3 use TPS56637 6A-class bucks with XAL7070 inductors; endpoint load budgets remain a release check."
- moved on the sheet: C2360, C2361, C2362, C2365, C44, C45, C768, C794, C830, R2280, R2363, R761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
